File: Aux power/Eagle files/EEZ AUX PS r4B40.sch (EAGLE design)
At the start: 45 parts, among them IC1 LM25575, Q1 BTA26-600, Q2 BTA26-600, X1 AC_IN, X2 22-23-2041, X3 22-23-2031

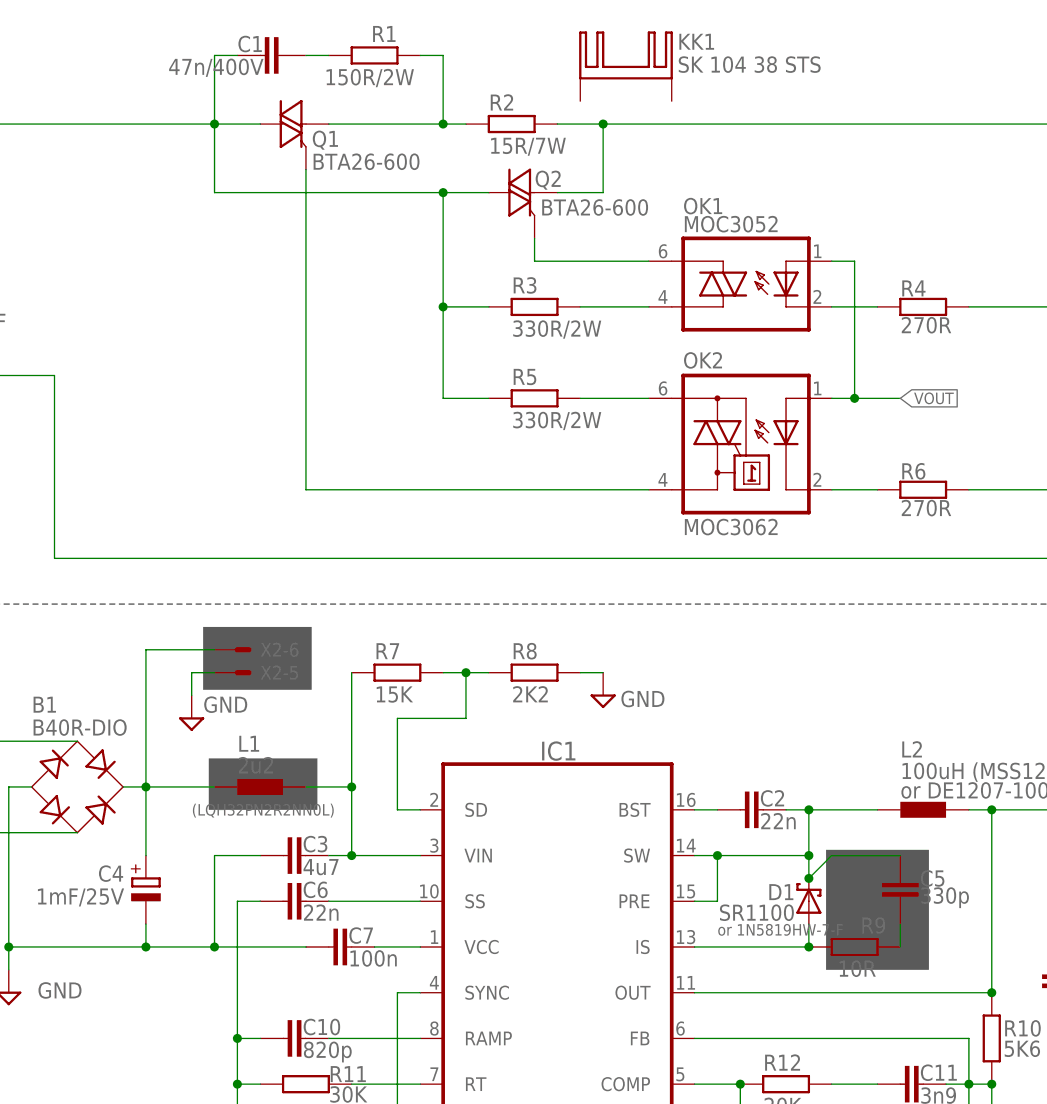
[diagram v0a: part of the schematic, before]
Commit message: AUX PS upgraded to r4B40
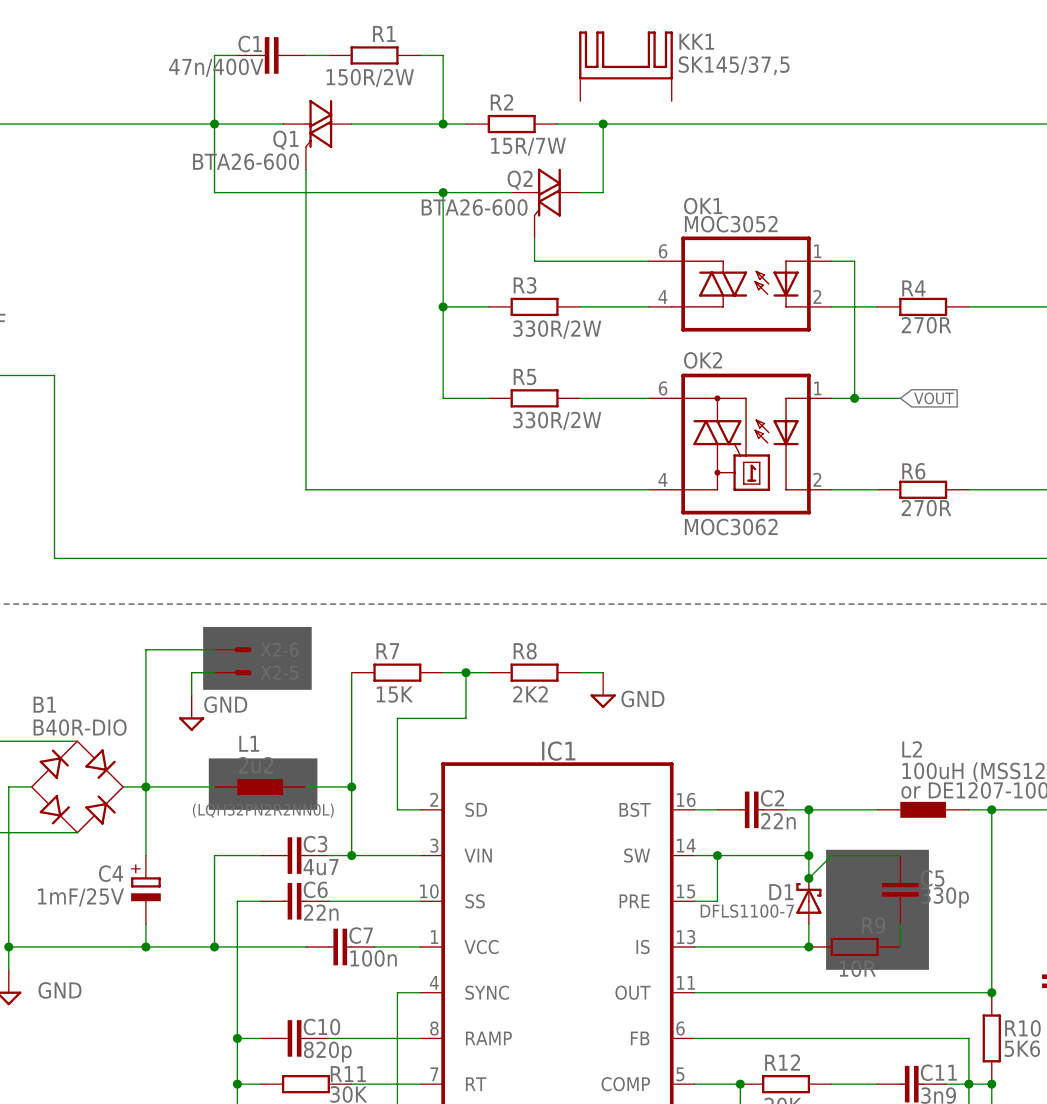
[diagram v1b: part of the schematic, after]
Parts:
- D1: value SR1100 -> DFLS1100-7; device EEZ_Lib1:SCHOTTKYDO34+SOD123 -> EEZ_Lib1:SCHOTTKYSOD123
- KK1: value SK 104 38 STS -> SK145/37,5; device EEZ_Lib1:SK409 -> EEZ_Lib1:SK145
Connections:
- net AC_IN1: now also Q1.A1, Q2.A1; no longer Q1.A2, Q2.A2
- net N$16: now also Q1.A2; no longer Q1.A1
- net N$8: now also Q2.A2; no longer Q2.A1
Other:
- note removed: "or 1N5819HW-7-F"
- moved on the sheet: Q1, Q2
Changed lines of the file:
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@@
 <setting verticaltext="up"/>
 </settings>
-<grid distance="0.025" unitdist="inch" unit="inch" style="lines" multiple="1" display="no" altdistance="0.01" altunitdist="inch" altunit="inch"/>
+<grid distance="0.1" unitdist="inch" unit="inch" style="lines" multiple="1" display="no" altdistance="0.01" altunitdist="inch" altunit="inch"/>
 <layers>
 <layer number="1" name="Top" color="4" fill="1" visible="no" active="no"/>
@@
 <layer number="97" name="Info" color="8" fill="1" visible="yes" active="yes"/>
 <layer number="98" name="Guide" color="6" fill="1" visible="yes" active="yes"/>
+<layer number="99" name="SpiceOrder" color="5" fill="1" visible="no" active="no"/>
 <layer number="100" name="Measurement" color="12" fill="1" visible="yes" active="yes"/>
 <layer number="101" name="Pinouts" color="13" fill="1" visible="yes" active="yes"/>
@@
 </variantdefs>
 <classes>
-<class number="0" name="default" width="0.254" drill="0.6096">
+<class number="0" name="default" width="0.254" drill="0.5842">
 </class>
-<class number="2" name="gnd" width="0.254" drill="0.6096">
+<class number="2" name="gnd" width="0.254" drill="0.5842">
 <clearance class="2" value="0.254"/>
 </class>
@@
 <part name="C7" library="rcl" deviceset="C-EU" device="C0805" value="100n"/>
 <part name="C6" library="rcl" deviceset="C-EU" device="C0805" value="22n"/>
-<part name="D1" library="EEZ_Lib1" deviceset="SCHOTTKY" device="DO34+SOD123" value="SR1100"/>
+<part name="D1" library="EEZ_Lib1" deviceset="SCHOTTKY" device="SOD123" value="DFLS1100-7"/>
 <part name="IC1" library="EEZ_Lib1" deviceset="LM(2)5575" device="" value="LM25575"/>
 <part name="C3" library="rcl" deviceset="C-EU" device="C1210" value="4u7"/>
@@
 <part name="C1" library="rcl" deviceset="C-EU" device="075-052X106" value="47n/400V"/>
 <part name="R2" library="EEZ_Lib1" deviceset="R_EU" device="7W" value="15R/7W"/>
-<part name="KK1" library="EEZ_Lib1" deviceset="SK409" device="" value="SK 104 38 STS "/>
+<part name="KK1" library="EEZ_Lib1" deviceset="SK145" device="" value="SK145/37,5"/>
 <part name="OK1" library="EEZ_Lib1" deviceset="MOC305X" device="" value="MOC3052"/>
 <part name="OK2" library="optocoupler" deviceset="MOC30*" device="S" technology="33" value="MOC3062">
@@
 <text x="12.7" y="123.19" size="1.778" layer="97" rot="R180">Earth</text>
 <text x="165.1" y="90.17" size="1.778" layer="96">or DE1207-100 </text>
-<text x="144.78" y="74.93" size="1.27" layer="96">or 1N5819HW-7-F</text>
 <text x="198.12" y="163.83" size="1.778" layer="97">Line out</text>
 <text x="198.12" y="118.11" size="1.778" layer="97">Neutral out</text>
@@
 <instance part="D1" gate="G$1" x="154.94" y="78.74" smashed="yes" rot="R90">
 <attribute name="NAME" x="153.416" y="80.645" size="1.778" layer="95" rot="R180"/>
-<attribute name="VALUE" x="153.416" y="78.359" size="1.778" layer="96" rot="R180"/>
+<attribute name="VALUE" x="153.416" y="78.359" size="1.4224" layer="96" rot="R180"/>
 </instance>
 <instance part="IC1" gate="G$1" x="127" y="71.12" smashed="yes">
@@
 <attribute name="VALUE" x="91.44" y="92.964" size="1.778" layer="96"/>
 </instance>
-<instance part="Q1" gate="-1" x="99.06" y="165.1" smashed="yes" rot="R90">
-<attribute name="NAME" x="99.695" y="162.56" size="1.778" layer="95"/>
-<attribute name="VALUE" x="99.695" y="160.02" size="1.778" layer="96"/>
-</instance>
-<instance part="Q2" gate="-1" x="124.46" y="157.48" smashed="yes" rot="R90">
-<attribute name="NAME" x="124.46" y="158.115" size="1.778" layer="95"/>
-<attribute name="VALUE" x="125.095" y="154.94" size="1.778" layer="96"/>
+<instance part="Q1" gate="-1" x="99.06" y="165.1" smashed="yes" rot="MR90">
+<attribute name="NAME" x="98.425" y="162.56" size="1.778" layer="95" rot="MR0"/>
+<attribute name="VALUE" x="98.425" y="160.02" size="1.778" layer="96" rot="MR0"/>
+</instance>
+<instance part="Q2" gate="-1" x="124.46" y="157.48" smashed="yes" rot="MR90">
+<attribute name="NAME" x="124.46" y="158.115" size="1.778" layer="95" rot="MR0"/>
+<attribute name="VALUE" x="123.825" y="154.94" size="1.778" layer="96" rot="MR0"/>
 </instance>
 <instance part="R5" gate="G$1" x="124.46" y="134.62" smashed="yes" rot="R180">
@@
 <junction x="33.02" y="165.1"/>
 <label x="19.685" y="165.735" size="1.27" layer="102"/>
-<pinref part="Q1" gate="-1" pin="A2"/>
-<pinref part="Q2" gate="-1" pin="A2"/>
-<wire x1="88.9" y1="165.1" x2="93.98" y2="165.1" width="0.1524" layer="91"/>
-<wire x1="119.38" y1="157.48" x2="114.3" y2="157.48" width="0.1524" layer="91"/>
 <wire x1="114.3" y1="157.48" x2="88.9" y2="157.48" width="0.1524" layer="91"/>
 <wire x1="88.9" y1="157.48" x2="88.9" y2="165.1" width="0.1524" layer="91"/>
@@
 <wire x1="119.38" y1="144.78" x2="114.3" y2="144.78" width="0.1524" layer="91"/>
 <wire x1="114.3" y1="144.78" x2="114.3" y2="157.48" width="0.1524" layer="91"/>
-<junction x="114.3" y="157.48"/>
 <wire x1="114.3" y1="134.62" x2="114.3" y2="144.78" width="0.1524" layer="91"/>
 <junction x="114.3" y="144.78"/>
@@
 <wire x1="88.9" y1="172.72" x2="91.44" y2="172.72" width="0.1524" layer="91"/>
 <wire x1="88.9" y1="165.1" x2="88.9" y2="172.72" width="0.1524" layer="91"/>
+<pinref part="Q1" gate="-1" pin="A1"/>
+<wire x1="96.52" y1="165.1" x2="88.9" y2="165.1" width="0.1524" layer="91"/>
+<pinref part="Q2" gate="-1" pin="A1"/>
+<wire x1="114.3" y1="157.48" x2="121.92" y2="157.48" width="0.1524" layer="91"/>
+<junction x="114.3" y="157.48"/>
 </segment>
 <segment>
@@
 <net name="N$8" class="0">
 <segment>
-<pinref part="Q2" gate="-1" pin="A1"/>
-<wire x1="127" y1="157.48" x2="132.08" y2="157.48" width="0.1524" layer="91"/>
 <wire x1="132.08" y1="157.48" x2="132.08" y2="165.1" width="0.1524" layer="91"/>
 <wire x1="132.08" y1="165.1" x2="193.04" y2="165.1" width="0.1524" layer="91"/>
@@
 <wire x1="127" y1="165.1" x2="132.08" y2="165.1" width="0.1524" layer="91"/>
 <junction x="132.08" y="165.1"/>
+<pinref part="Q2" gate="-1" pin="A2"/>
+<wire x1="129.54" y1="157.48" x2="132.08" y2="157.48" width="0.1524" layer="91"/>
 </segment>
 </net>
@@
 <net name="N$16" class="0">
 <segment>
-<pinref part="Q1" gate="-1" pin="A1"/>
-<wire x1="101.6" y1="165.1" x2="114.3" y2="165.1" width="0.1524" layer="91"/>
 <pinref part="R2" gate="G$1" pin="1"/>
 <pinref part="R1" gate="G$1" pin="2"/>
@@
 <wire x1="111.76" y1="172.72" x2="114.3" y2="172.72" width="0.1524" layer="91"/>
 <wire x1="114.3" y1="165.1" x2="114.3" y2="172.72" width="0.1524" layer="91"/>
+<pinref part="Q1" gate="-1" pin="A2"/>
+<wire x1="104.14" y1="165.1" x2="114.3" y2="165.1" width="0.1524" layer="91"/>
 <junction x="114.3" y="165.1"/>
 </segment>
